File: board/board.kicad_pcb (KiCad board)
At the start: 2 copper layers, 44 x 29 mm, 3 parts, among them U1 RP2040, U2 W25Q128JVS

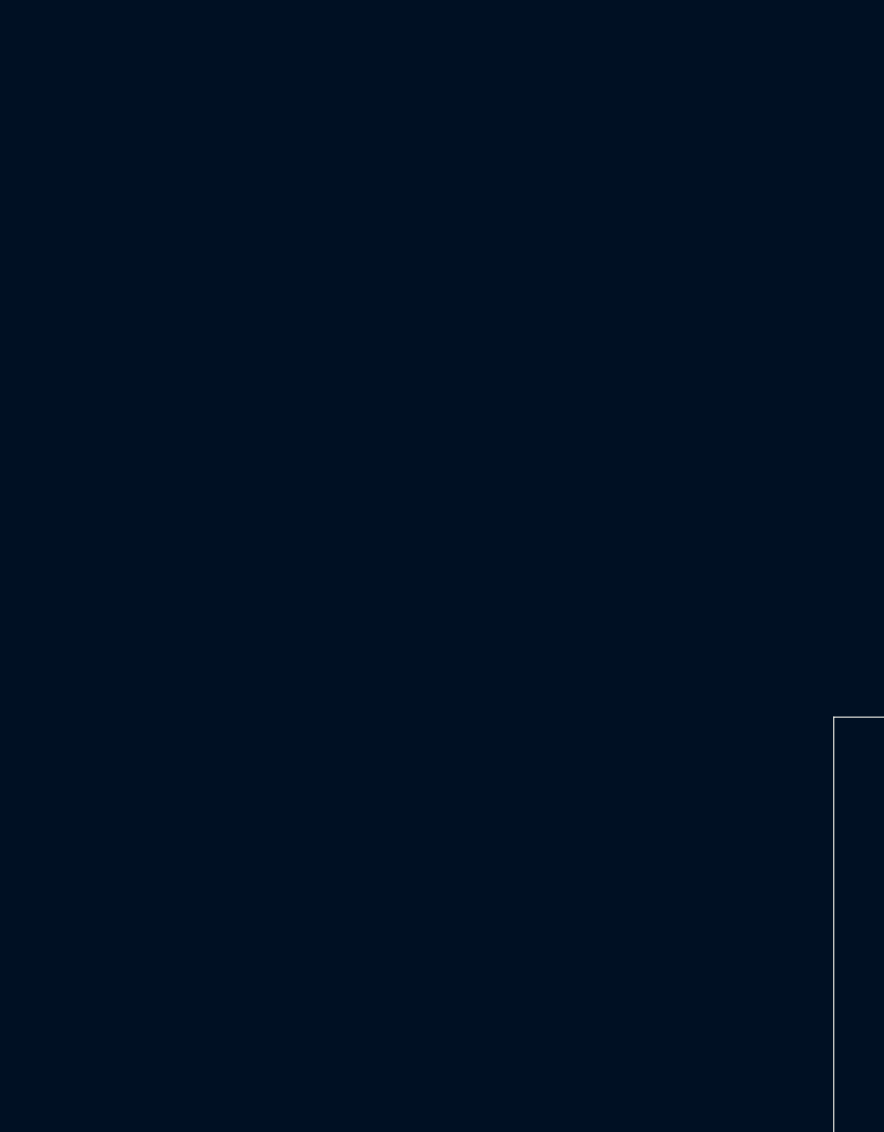
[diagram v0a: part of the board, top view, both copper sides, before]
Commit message: implement proper usb C
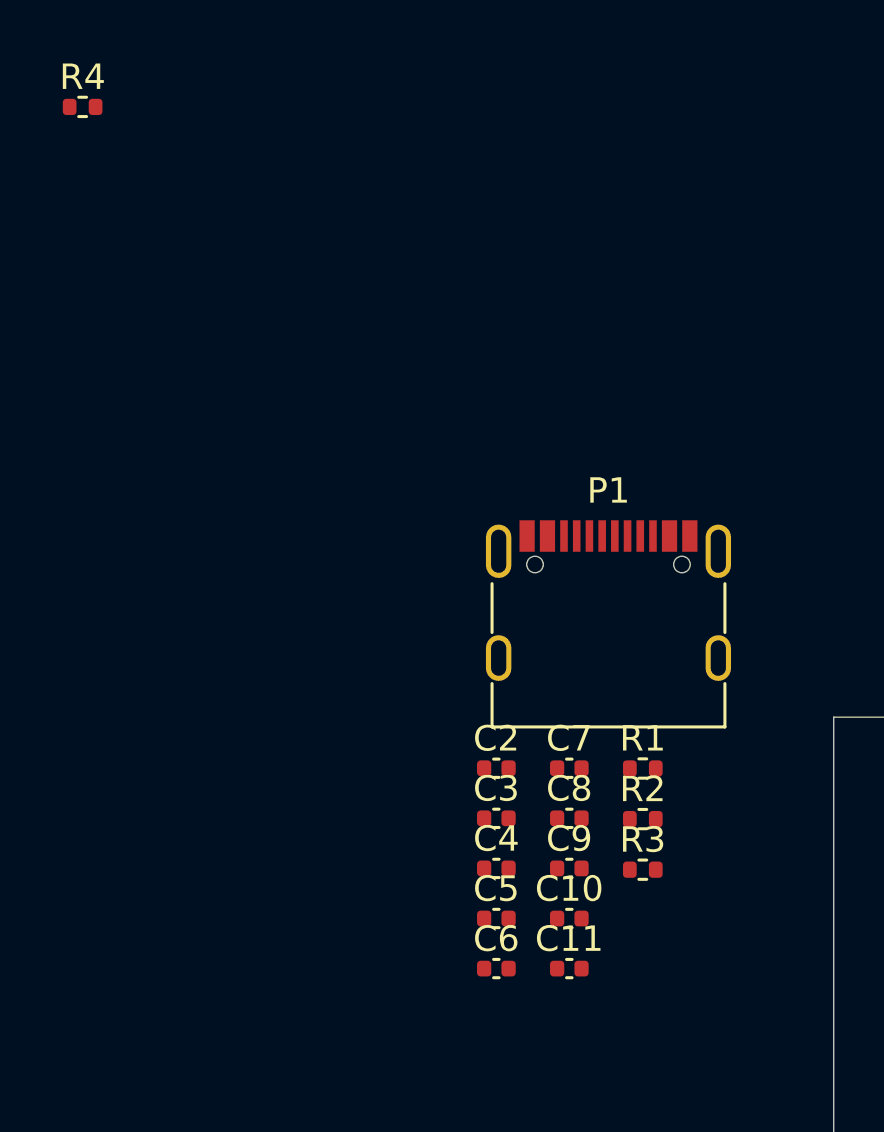
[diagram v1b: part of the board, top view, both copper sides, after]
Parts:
- added C10: 100nF, Capacitor_SMD:C_0402_1005Metric, F.Cu at (20.1, 32.4)
- added C11: 1uF, Capacitor_SMD:C_0402_1005Metric, F.Cu at (20.1, 34.4)
- added C2: 100nF, Capacitor_SMD:C_0402_1005Metric, F.Cu at (17.2, 26.5)
- added C3: 100nF, Capacitor_SMD:C_0402_1005Metric, F.Cu at (17.2, 28.5)
- added C4: 100nF, Capacitor_SMD:C_0402_1005Metric, F.Cu at (17.2, 30.4)
- added C5: 100nF, Capacitor_SMD:C_0402_1005Metric, F.Cu at (17.2, 32.4)
- added C6: 100nF, Capacitor_SMD:C_0402_1005Metric, F.Cu at (17.2, 34.4)
- added C7: 100nF, Capacitor_SMD:C_0402_1005Metric, F.Cu at (20.1, 26.5)
- added C8: 1uF, Capacitor_SMD:C_0402_1005Metric, F.Cu at (20.1, 28.5)
- added C9: 100nF, Capacitor_SMD:C_0402_1005Metric, F.Cu at (20.1, 30.4)
- added P1: USB_C_Plug_USB2.0, Connector_USB:USB_C_Receptacle_G-Switch_GT-USB-7010ASV, F.Cu at (21.6, 21.1)
- added R1: 27.4, Resistor_SMD:R_0402_1005Metric, F.Cu at (23.0, 26.5)
- added R2: 27.4, Resistor_SMD:R_0402_1005Metric, F.Cu at (23.0, 28.5)
- added R3: 5.1k, Resistor_SMD:R_0402_1005Metric, F.Cu at (23.0, 30.5)
- added R4: 5.1k, Resistor_SMD:R_0402_1005Metric, F.Cu at (0.95, 0.49)
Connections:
- C1 pad 2: VCC -> +3V3
- U1 pad 1: VCC -> +3V3
- U1 pad 10: VCC -> +3V3
- U1 pad 19: unconnected-(U1-TESTEN-Pad19) -> GND
- U1 pad 22: VCC -> +3V3
- U1 pad 23: Net-(U1-DVDD-Pad23) -> +1V1
- U1 pad 33: VCC -> +3V3
- U1 pad 42: VCC -> +3V3
- U1 pad 43: unconnected-(U1-ADC_AVDD-Pad43) -> +3V3
- U1 pad 44: unconnected-(U1-VREG_IN-Pad44) -> +3V3
- U1 pad 45: unconnected-(U1-VREG_VOUT-Pad45) -> +1V1
- U1 pad 46: unconnected-(U1-USB_DM-Pad46) -> Net-(U1-USB_DM)
- U1 pad 47: unconnected-(U1-USB_DP-Pad47) -> Net-(U1-USB_DP)
- U1 pad 48: unconnected-(U1-USB_VDD-Pad48) -> +3V3
- U1 pad 49: VCC -> +3V3
- U1 pad 50: Net-(U1-DVDD-Pad23) -> +1V1
- U1 pad 51: unconnected-(U1-QSPI_SD3-Pad51) -> Net-(U1-QSPI_SD3)
- U1 pad 52: unconnected-(U1-QSPI_SCLK-Pad52) -> Net-(U1-QSPI_SCLK)
- U1 pad 53: unconnected-(U1-QSPI_SD0-Pad53) -> Net-(U1-QSPI_SD0)
- U1 pad 54: unconnected-(U1-QSPI_SD2-Pad54) -> Net-(U1-QSPI_SD2)
- U1 pad 55: unconnected-(U1-QSPI_SD1-Pad55) -> Net-(U1-QSPI_SD1)
- U1 pad 56: unconnected-(U1-QSPI_SS-Pad56) -> Net-(U1-QSPI_SS)
- U1 pad 57: unconnected-(U1-GND-Pad57) -> GND
- U2 pad 1: unconnected-(U2-~{CS}-Pad1) -> Net-(U1-QSPI_SS)
- U2 pad 2: unconnected-(U2-DO(IO1)-Pad2) -> Net-(U1-QSPI_SD1)
- U2 pad 3: unconnected-(U2-IO2-Pad3) -> Net-(U1-QSPI_SD2)
- U2 pad 4: unconnected-(U2-GND-Pad4) -> GND
- U2 pad 5: unconnected-(U2-DI(IO0)-Pad5) -> Net-(U1-QSPI_SD0)
- U2 pad 6: unconnected-(U2-CLK-Pad6) -> Net-(U1-QSPI_SCLK)
- U2 pad 7: unconnected-(U2-IO3-Pad7) -> Net-(U1-QSPI_SD3)
- U2 pad 8: unconnected-(U2-VCC-Pad8) -> +3V3

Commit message: board design: hr1
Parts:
- added C12: 10uF, Capacitor_SMD:C_0402_1005Metric, F.Cu at (62.6, 59.5)
- added C13: 10uF, Capacitor_SMD:C_0402_1005Metric, F.Cu at (62.6, 61.5)
- added C14: 100nF, Capacitor_SMD:C_0402_1005Metric, F.Cu at (62.6, 63.5)
- added C15: 15pF, Capacitor_SMD:C_0402_1005Metric, F.Cu at (62.6, 65.4)
- added C16: 15pF, Capacitor_SMD:C_0402_1005Metric, F.Cu at (71.5, 57.5)
- added J1: ANT, Connector_Coaxial:U.FL_Hirose_U.FL-R-SMT-1_Vertical, F.Cu at (52.0, 75.0)
- added J2: DEBUG, Connector_PinSocket_2.54mm:PinSocket_1x02_P2.54mm_Vertical, F.Cu at (85.0, 55.0)
- added R5: 10k, Resistor_SMD:R_0402_1005Metric, F.Cu at (65.5, 59.5)
- added R6: 1k, Resistor_SMD:R_0402_1005Metric, F.Cu at (65.5, 61.5)
- added R7: 1k, Resistor_SMD:R_0402_1005Metric, F.Cu at (65.5, 63.5)
- added R8: 10k, Resistor_SMD:R_0402_1005Metric, F.Cu at (65.5, 65.5)
- added SW1: BOOTSEL, Button_Switch_SMD:SW_Push_SPST_NO_Alps_SKRK, F.Cu at (71.0, 64.0)
- added SW2: RUN, Button_Switch_SMD:SW_Push_SPST_NO_Alps_SKRK, F.Cu at (75.0, 72.0)
- added U3: NCP1117-3.3_SOT223, Package_TO_SOT_SMD:SOT-223-3_TabPin2, F.Cu at (36.0, 38.5)
- added U4: RFM95W-915S2, RF_Module:HOPERF_RFM9XW_SMD, F.Cu at (36.5, 66.0)
- added Y1: ABM8G-12.000MHZ-18-D2Y-T, Crystal:Crystal_SMD_Abracon_ABM8G-4Pin_3.2x2.5mm, F.Cu at (-7.60, 55.1)
- moved R4 45.4 mm to (35.5, 30.0), turned to -90 degrees
- moved U2 31.6 mm to (72.0, 25.5)
- moved U1 18.4 mm to (72.0, 50.0)
- moved R3 15.5 mm to (38.5, 30.0), turned to -90 degrees
- moved P1 15.4 mm to (37.0, 22.0), turned to 180 degrees
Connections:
- U1 pad 11: unconnected-(U1-GPIO8-Pad11) -> /DIO4
- U1 pad 12: unconnected-(U1-GPIO9-Pad12) -> /DIO5
- U1 pad 13: unconnected-(U1-GPIO10-Pad13) -> Net-(U1-GPIO10)
- U1 pad 2: unconnected-(U1-GPIO0-Pad2) -> Net-(U1-GPIO0)
- U1 pad 20: unconnected-(U1-XIN-Pad20) -> Net-(U1-XIN)
- U1 pad 21: unconnected-(U1-XOUT-Pad21) -> Net-(U1-XOUT)
- U1 pad 24: unconnected-(U1-SWCLK-Pad24) -> Net-(J2-Pin_2)
- U1 pad 25: unconnected-(U1-SWD-Pad25) -> Net-(J2-Pin_1)
- U1 pad 26: unconnected-(U1-RUN-Pad26) -> Net-(U1-RUN)
- U1 pad 3: unconnected-(U1-GPIO1-Pad3) -> Net-(U1-GPIO1)
- U1 pad 4: unconnected-(U1-GPIO2-Pad4) -> Net-(U1-GPIO2)
- U1 pad 5: unconnected-(U1-GPIO3-Pad5) -> Net-(U1-GPIO3)
- U1 pad 6: unconnected-(U1-GPIO4-Pad6) -> /DIO0
- U1 pad 7: unconnected-(U1-GPIO5-Pad7) -> /DIO1
- U1 pad 8: unconnected-(U1-GPIO6-Pad8) -> /DIO2
- U1 pad 9: unconnected-(U1-GPIO7-Pad9) -> /DIO3
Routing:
- net GND: track 0.00 -> 3.80 mm, vias 0 -> 2
- added copper zone on In1.Cu, net +3V3
- added copper zone on In2.Cu, net GND
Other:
- board outline removed
- copper layers 2 -> 4

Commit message: board design: hr2
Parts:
- U3: value NCP1117-3.3_SOT223 -> NCP1117
- Y1: value ABM8G-12.000MHZ-18-D2Y-T -> ABM8G
- moved Y1 76.6 mm to (68.9, 59.9)
- moved C2 66.0 mm to (78.5, 51.0), turned to 180 degrees
- moved C3 61.5 mm to (72.0, 56.5), turned to 90 degrees
- moved C7 58.3 mm to (75.5, 44.5), turned to -90 degrees
- moved C6 56.1 mm to (72.5, 44.0), turned to -90 degrees
- moved C4 52.4 mm to (65.0, 52.0)
- moved C5 51.6 mm to (67.0, 46.0), turned to -90 degrees
- moved C1 28.0 mm to (77.5, 46.5), turned to 180 degrees
- moved C12 27.6 mm to (46.0, 37.5), turned to 90 degrees
- moved R6 24.3 mm to (85.0, 47.0)
- moved R5 22.4 mm to (85.0, 48.5), turned to 180 degrees
- moved C13 21.5 mm to (84.0, 64.0)
- moved C14 21.5 mm to (84.0, 66.0)
- moved R8 21.5 mm to (86.9, 68.0)
- moved SW2 21.0 mm to (96.0, 72.5)
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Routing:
- net GND: track 3.80 -> 93.3 mm, vias 2 -> 4
- net +3V3: track 0.00 -> 56.5 mm
- net Net-(U1-QSPI_SS): track 0.00 -> 37.2 mm, vias 0 -> 2
- net VBUS: track 0.00 -> 21.8 mm
- net /DIO1: track 0.00 -> 21.7 mm
- net Net-(U1-QSPI_SD2): track 0.00 -> 17.3 mm, vias 0 -> 2
- net Net-(U1-QSPI_SD1): track 0.00 -> 16.9 mm, vias 0 -> 2
- net /DIO3: track 0.00 -> 16.6 mm, vias 0 -> 2
- net /DIO2: track 0.00 -> 15.2 mm
- net /DIO4: track 0.00 -> 13.7 mm
- net /DIO0: track 0.00 -> 13.2 mm, vias 0 -> 2
- net Net-(U1-QSPI_SD3): track 0.00 -> 12.8 mm
- net Net-(U1-QSPI_SCLK): track 0.00 -> 11.4 mm
- net Net-(U1-XOUT): track 0.00 -> 10.8 mm
- net Net-(U1-QSPI_SD0): track 0.00 -> 9.47 mm
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- removed copper zone on In1.Cu, net +3V3
- removed copper zone on In2.Cu, net GND
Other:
- copper layers 4 -> 2

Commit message: board design v1
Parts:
- moved C9 59.6 mm to (74.0, 56.0), turned to -90 degrees
- moved C8 57.6 mm to (76.0, 42.5), turned to 90 degrees
- moved C11 54.6 mm to (74.5, 44.0), turned to 90 degrees
- moved R1 54.1 mm to (75.0, 41.5), turned to -90 degrees
- moved C10 52.8 mm to (72.0, 42.0), turned to 90 degrees
- moved R2 52.2 mm to (73.5, 41.5), turned to -90 degrees
- moved C13 37.2 mm to (56.5, 39.0), turned to -90 degrees
- moved SW2 23.4 mm to (79.4, 56.0), turned to 180 degrees
- moved R8 23.1 mm to (67.5, 55.5), turned to 90 degrees
- moved C14 13.7 mm to (81.5, 52.5)
- moved J2 10.7 mm to (83.5, 63.0), turned to 0 degrees
- moved C4 1.00 mm to (65.0, 51.0)
- moved C7 1.00 mm to (76.5, 44.5)
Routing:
- net GND: track 93.3 -> 203.4 mm, vias 4 -> 11
- net +3V3: track 56.5 -> 130.4 mm, vias 0 -> 5
- net Net-(P1-D+-PadA6): track 0.00 -> 40.6 mm, vias 0 -> 2
- net Net-(P1-D--PadA7): track 0.00 -> 39.6 mm, vias 0 -> 2
- net Net-(U1-GPIO1): track 0.00 -> 33.5 mm, vias 0 -> 2
- net Net-(U1-GPIO2): track 0.00 -> 31.3 mm, vias 0 -> 2
- net Net-(U1-GPIO10): track 0.00 -> 31.0 mm, vias 0 -> 2
- net /DIO5: track 0.00 -> 30.3 mm, vias 0 -> 2
- net Net-(U1-GPIO0): track 0.00 -> 30.1 mm, vias 0 -> 2
- net Net-(U1-GPIO3): track 0.00 -> 28.6 mm, vias 0 -> 2
- net +1V1: track 0.00 -> 26.3 mm, vias 0 -> 2
- net Net-(J2-Pin_2): track 0.00 -> 21.1 mm, vias 0 -> 2
- net Net-(J2-Pin_1): track 0.00 -> 16.4 mm, vias 0 -> 2
- net Net-(U1-USB_DM): track 0.00 -> 5.35 mm
- net Net-(U1-RUN): track 0.00 -> 4.87 mm
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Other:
- board outline added: 53 x 42 mm
- board text added: "YARLo design by scarlettekk v1"

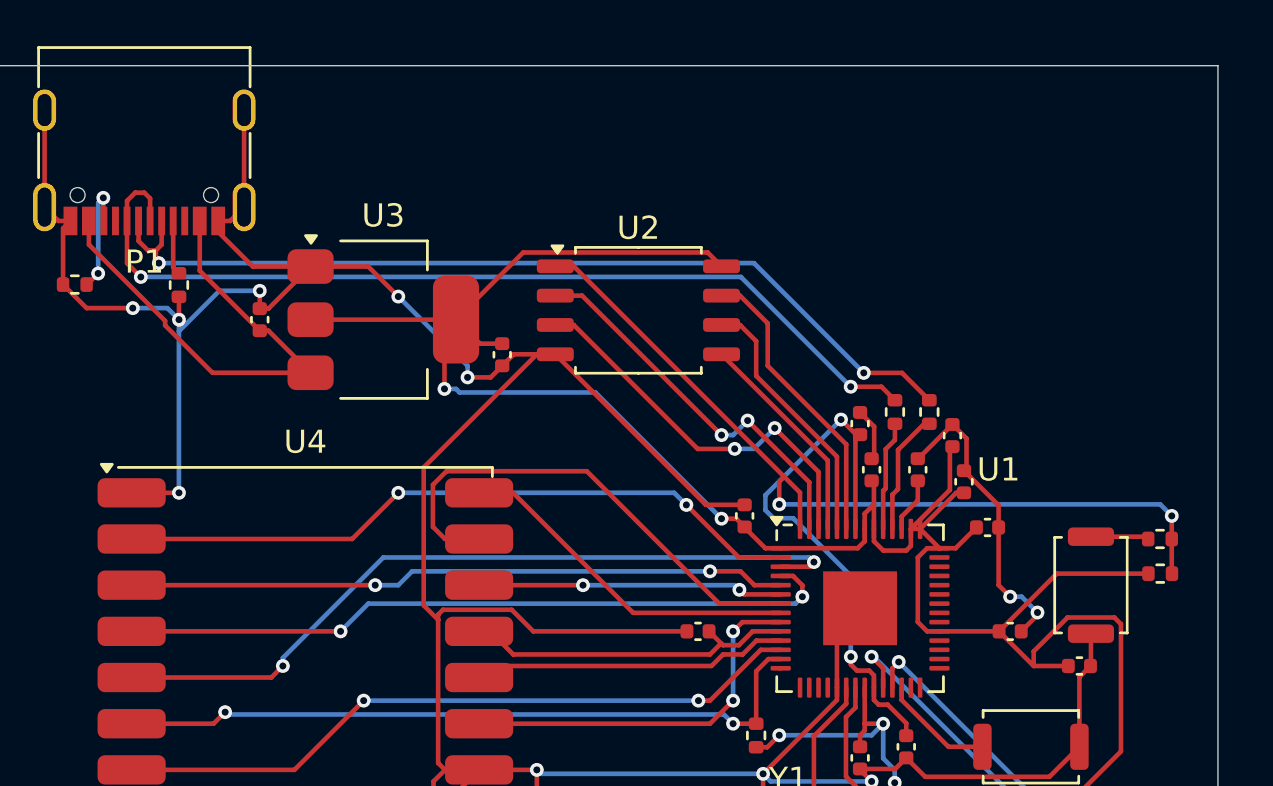
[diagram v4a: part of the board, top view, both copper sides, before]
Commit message: add GPIO
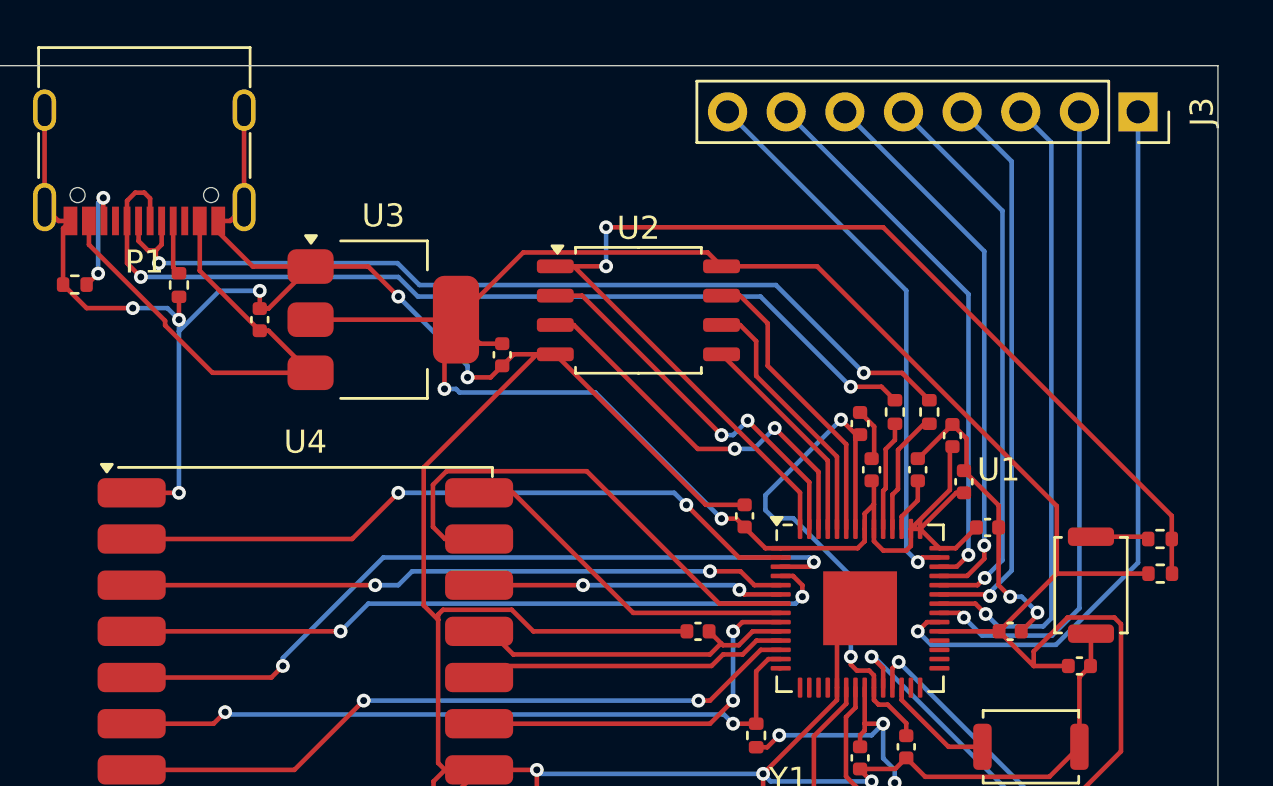
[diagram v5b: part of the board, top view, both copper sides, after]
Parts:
- added J3: GPIO, Connector_PinSocket_2.54mm:PinSocket_1x08_P2.54mm_Vertical, F.Cu at (84.0, 28.5)
- U3: value NCP1117 -> NCP1117-3.3_SOT223
- Y1: value ABM8G -> ABM8G-12.000MHZ-18-D2Y-T
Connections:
- U1 pad 34: unconnected-(U1-GPIO22-Pad34) -> Net-(J3-Pin_1)
- U1 pad 35: unconnected-(U1-GPIO23-Pad35) -> Net-(J3-Pin_2)
- U1 pad 36: unconnected-(U1-GPIO24-Pad36) -> Net-(J3-Pin_3)
- U1 pad 37: unconnected-(U1-GPIO25-Pad37) -> Net-(J3-Pin_4)
- U1 pad 38: unconnected-(U1-GPIO26_ADC0-Pad38) -> Net-(J3-Pin_5)
- U1 pad 39: unconnected-(U1-GPIO27_ADC1-Pad39) -> Net-(J3-Pin_6)
- U1 pad 40: unconnected-(U1-GPIO28_ADC2-Pad40) -> Net-(J3-Pin_7)
- U1 pad 41: unconnected-(U1-GPIO29_ADC3-Pad41) -> Net-(J3-Pin_8)
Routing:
- net Net-(J3-Pin_1): track 0.00 -> 31.9 mm, vias 0 -> 1
- net Net-(J3-Pin_2): track 0.00 -> 28.5 mm, vias 0 -> 1
- net Net-(J3-Pin_3): track 0.00 -> 27.9 mm, vias 0 -> 1
- net Net-(J3-Pin_4): track 0.00 -> 24.7 mm, vias 0 -> 1
- net Net-(J3-Pin_5): track 0.00 -> 24.4 mm, vias 0 -> 1
- net Net-(J3-Pin_6): track 0.00 -> 24.1 mm, vias 0 -> 1
- net Net-(J3-Pin_8): track 0.00 -> 23.9 mm, vias 0 -> 1
- net Net-(J3-Pin_7): track 0.00 -> 23.9 mm, vias 0 -> 1
- net +3V3: track 130.4 -> 147.2 mm
- net Net-(U1-QSPI_SS): track 37.2 -> 52.3 mm

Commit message: board v2 hour 1
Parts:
- added U5: BLE5201, BLE5201:BLE5201, F.Cu at (85.5, 37.8)
- J2: footprint Connector_PinSocket_2.54mm:PinSocket_1x02_P2.54mm_Vertical -> Connector_PinSocket_2.54mm:PinSocket_1x04_P2.54mm_Vertical
- J3: footprint Connector_PinSocket_2.54mm:PinSocket_1x08_P2.54mm_Vertical -> Connector_PinSocket_2.54mm:PinSocket_1x12_P2.54mm_Vertical
- moved R4 14.2 mm to (51.8, 39.5), turned to -90 degrees
- moved U2 10.5 mm to (72.9, 36.1)
- moved R3 9.31 mm to (51.8, 35.2), turned to 0 degrees
- moved U3 8.66 mm to (60.0, 37.0)
- moved P1 8.42 mm to (45.3, 36.8), turned to -90 degrees
- moved J2 7.64 mm to (75.9, 64.0), turned to 90 degrees
- moved C12 6.52 mm to (51.5, 34.0), turned to 0 degrees
- moved J1 5.37 mm to (60.5, 63.0)
- moved U4 5.05 mm to (53.0, 51.5)
- moved C13 2.84 mm to (54.5, 37.0), turned to 180 degrees
- moved R8 2.71 mm to (66.5, 53.0), turned to 0 degrees
- moved C10 1.60 mm to (71.5, 43.5)
- moved C3 1.57 mm to (73.5, 56.0)
- moved R7 1.13 mm to (71.5, 62.5)
- moved R1 1.01 mm to (74.0, 41.5)
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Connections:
- net Net-(U1-RUN) renamed /RUN
- U1 pad 14: unconnected-(U1-GPIO11-Pad14) -> Net-(U1-GPIO11)
- U1 pad 15: unconnected-(U1-GPIO12-Pad15) -> Net-(U1-GPIO12)
- U1 pad 16: unconnected-(U1-GPIO13-Pad16) -> Net-(U1-GPIO13)
- U1 pad 17: unconnected-(U1-GPIO14-Pad17) -> Net-(U1-GPIO14)
- U1 pad 18: unconnected-(U1-GPIO15-Pad18) -> /PB00
- U1 pad 27: unconnected-(U1-GPIO16-Pad27) -> /PB01
- U1 pad 28: unconnected-(U1-GPIO17-Pad28) -> /PB02
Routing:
- net GND: track 203.4 -> 52.9 mm, vias 11 -> 31
- net +3V3: track 147.2 -> 37.5 mm, vias 5 -> 7
- net Net-(P1-D+-PadA6): track 40.6 -> 0.00 mm, vias 2 -> 0
- net Net-(P1-D--PadA7): track 39.6 -> 0.00 mm, vias 2 -> 0
- net /BLE_SWCLK: track 0.00 -> 37.3 mm, vias 0 -> 1
- net /BLE_SWDIO: track 0.00 -> 35.9 mm, vias 0 -> 1
- net Net-(U1-GPIO1): track 33.5 -> 0.00 mm, vias 2 -> 0
- net Net-(J3-Pin_1): track 31.9 -> 0.00 mm, vias 1 -> 0
- net Net-(U1-GPIO2): track 31.3 -> 0.00 mm, vias 2 -> 0
- net /DIO5: track 30.3 -> 0.00 mm, vias 2 -> 0
- net Net-(U1-GPIO0): track 30.1 -> 0.00 mm, vias 2 -> 0
- net Net-(U1-GPIO10): track 31.0 -> 2.17 mm, vias 2 -> 0
- net Net-(U1-GPIO3): track 28.6 -> 0.00 mm, vias 2 -> 0
- net Net-(U1-QSPI_SS): track 52.3 -> 23.8 mm
- net Net-(J3-Pin_2): track 28.5 -> 0.00 mm, vias 1 -> 0
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- added copper zone on In2.Cu, net +3V3
- added copper zone on In1.Cu, net GND
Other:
- board size 53 x 42 mm -> 53 x 39.5 mm
- copper layers 2 -> 4
- board text removed: "YARLo design by scarlettekk v1"

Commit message: board v2 hour 2
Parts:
- moved C3 1.58 mm to (72.0, 56.5)
- moved C9 1.58 mm to (73.0, 56.5)
- moved C5 0.71 mm to (66.5, 45.5)
- moved C10 0.50 mm to (71.0, 43.5)
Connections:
- J3 pad 10: /PC01 -> unconnected-(J3-Pin_10-Pad10)
- J3 pad 11: /PC02 -> unconnected-(J3-Pin_11-Pad11)
- J3 pad 12: /PC03 -> unconnected-(J3-Pin_12-Pad12)
- J3 pad 9: /PC00 -> unconnected-(J3-Pin_9-Pad9)
- U5 pad 11: /PC00 -> unconnected-(U5-PC00-Pad11)
- U5 pad 12: /PC01 -> unconnected-(U5-PC01-Pad12)
- U5 pad 13: /PC02 -> unconnected-(U5-PC02-Pad13)
- U5 pad 14: /PC03 -> unconnected-(U5-PC03-Pad14)
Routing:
- net Net-(J3-Pin_1): track 0.00 -> 34.9 mm, vias 0 -> 3
- net Net-(J3-Pin_2): track 0.00 -> 31.7 mm, vias 0 -> 4
- net /PB00: track 0.00 -> 31.5 mm, vias 0 -> 2
- net Net-(P1-D--PadA7): track 0.00 -> 29.6 mm, vias 0 -> 2
- net Net-(U1-GPIO13): track 0.00 -> 29.6 mm, vias 0 -> 2
- net Net-(P1-D+-PadA6): track 0.00 -> 28.2 mm, vias 0 -> 2
- net Net-(J3-Pin_8): track 0.00 -> 27.9 mm, vias 0 -> 2
- net Net-(U1-GPIO12): track 0.00 -> 27.7 mm, vias 0 -> 2
- net Net-(U1-GPIO11): track 0.00 -> 27.6 mm, vias 0 -> 2
- net Net-(J3-Pin_4): track 0.00 -> 27.2 mm, vias 0 -> 2
- net Net-(J3-Pin_3): track 0.00 -> 26.5 mm, vias 0 -> 2
- net Net-(J3-Pin_5): track 0.00 -> 26.2 mm, vias 0 -> 2
- net Net-(U1-GPIO1): track 0.00 -> 25.9 mm, vias 0 -> 2
- net Net-(U1-GPIO0): track 0.00 -> 25.5 mm, vias 0 -> 2
- net Net-(J3-Pin_7): track 0.00 -> 25.4 mm, vias 0 -> 2
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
